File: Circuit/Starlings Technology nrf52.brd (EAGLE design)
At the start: 45.1 x 52.7 mm, 58 parts, among them J4 USB Micro, J7 CORTEX_DEBUG_SMD, Q2 BSS84, U2 MCP73831, U3 BC840M, U4 MIC5317 (MIC5205), U5 74AHCT2G125, U8 TPS61235P, Y2 FC-12M

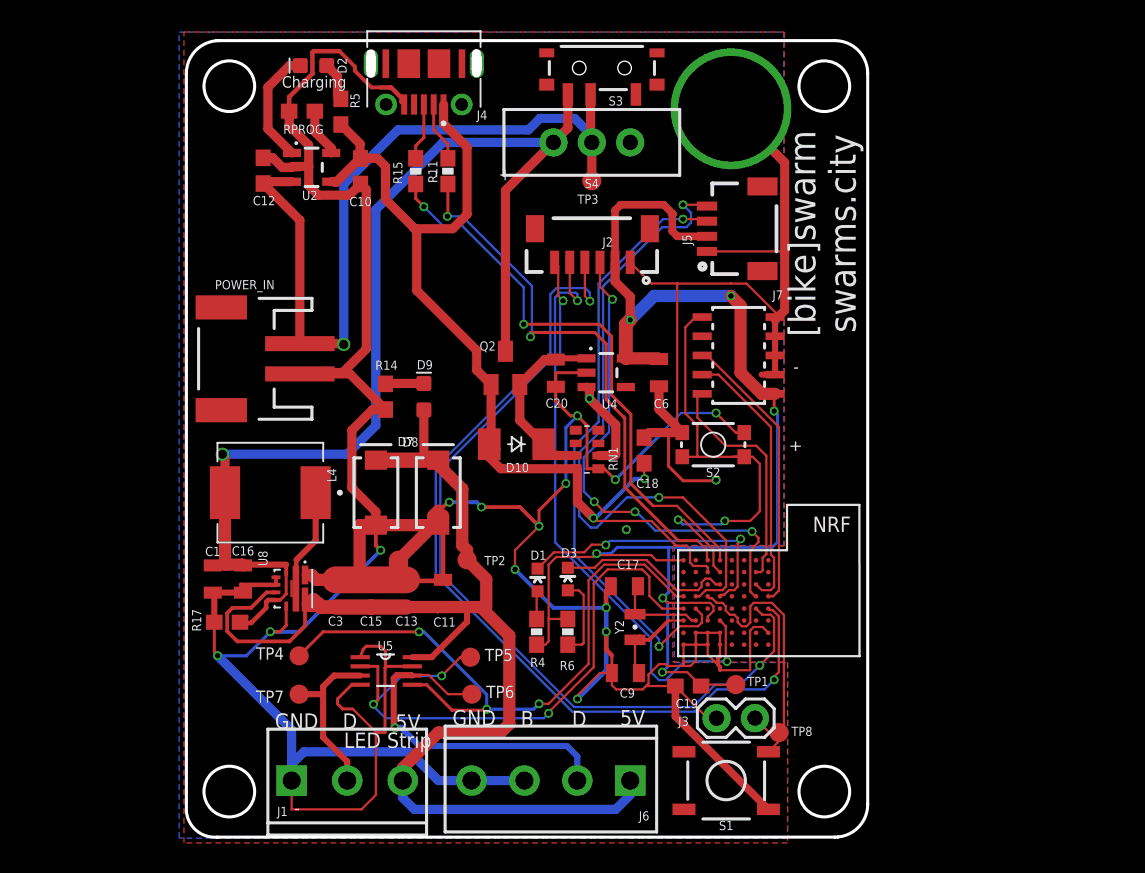
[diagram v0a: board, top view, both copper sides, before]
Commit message: Adding new rocker switch and two tactile switches. Footprints are drawn and ready, just needs routing.
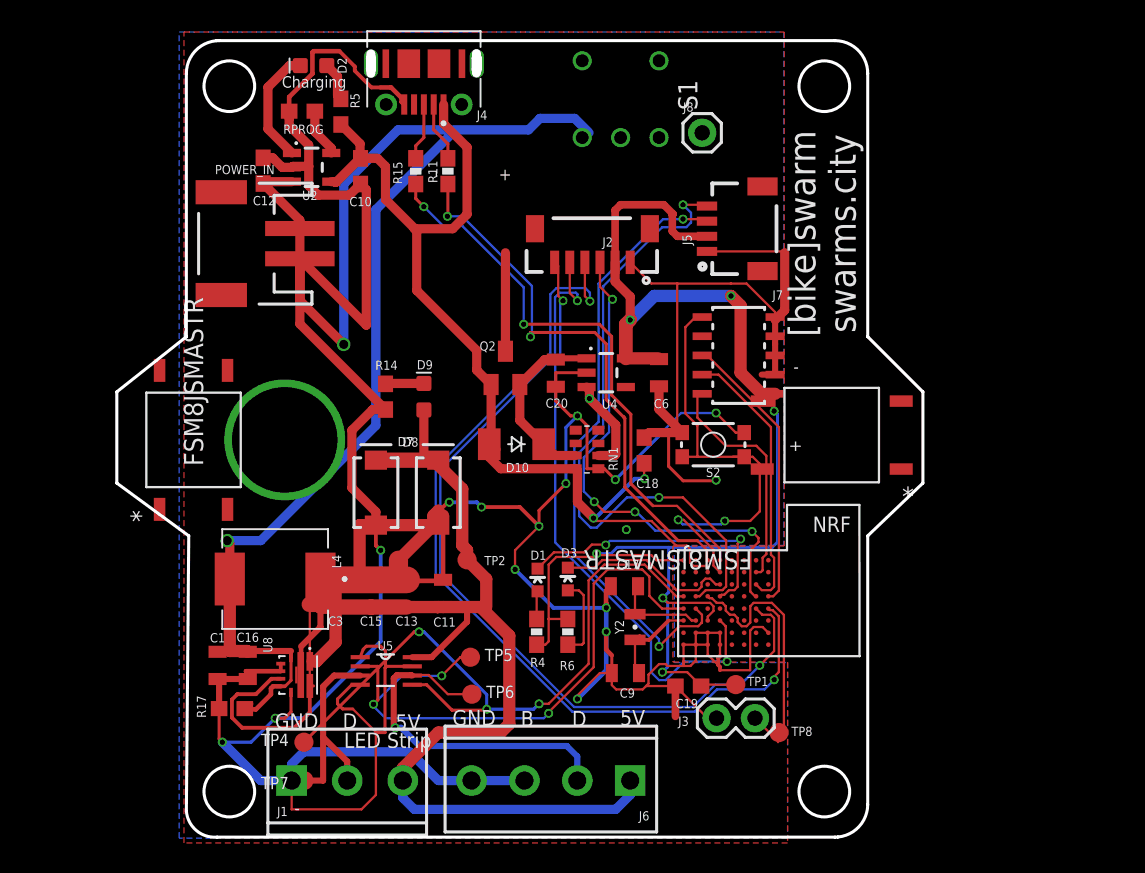
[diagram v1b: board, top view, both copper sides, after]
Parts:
- removed S3: (no value), SparkFun-Switches:SWITCH_SPST_SMD_A
- removed S4: (no value), SparkFun-Switches:SWITCH_SPDT_PTH_11.6X4.0MM
- removed TP3: TPSB1,27, testpad:B1,27
- added J8: (no value), SparkFun-Connectors:1X01
- added SW1, SW2: FSM8JSMASTR, FSM8JSMASTR:SW4_FSM8JSMASTR_TEC
- S1: value SPST-SMD-5.2MM -> CF-LD-1DC4-AR2W; device SparkFun-Switches:TACTILE_SWITCH_SMD_5.2MM -> RA1122DWR:CF-LD-1DC4-AR2W
- moved S1 45.6 mm to (24.8, 49.2), turned to 270 degrees
- moved POWER_IN 7.62 mm to (-0.16, 39.7)
- moved L4 5.72 mm to (1.91, 17.5)
- moved R17 5.72 mm to (-0.95, 8.89)
- moved TP4 5.72 mm to (3.81, 6.67)
- moved U8 5.72 mm to (3.43, 11.1)
- moved TP7 5.72 mm to (3.81, 4.13)
- moved C1 5.72 mm to (-1.91, 11.7)
- moved C16 5.72 mm to (0.10, 11.7)
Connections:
- new net 6: S1.5
- new net SWITCH_2: SW2.3, SW2.4
- net GND: now also SW1.1, SW1.2, SW2.1, SW2.2; no longer S1.1
- net SWITCH_1: now also SW1.3, SW1.4; no longer S1.3
- net VBAT: now also J8.1, S1.3; no longer S3.1, S4.1
- net VBAT_RAW: now also S1.4; no longer S3.2, S4.2, TP3.TP
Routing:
- net VBAT: track 77.8 -> 61.3 mm
- net GND: track 350.6 -> 340.7 mm
- net VBAT_RAW: track 52.1 -> 43.9 mm
- net 5V: track 90.3 -> 95.6 mm
- net HEADLAMP_5V: track 11.2 -> 13.8 mm
- net HEADLAMP_3V3: track 43.6 -> 45.6 mm
- net SWITCH_1: track 19.5 -> 18.6 mm
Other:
- board size 45.1 x 52.7 mm -> 53.3 x 52.7 mm

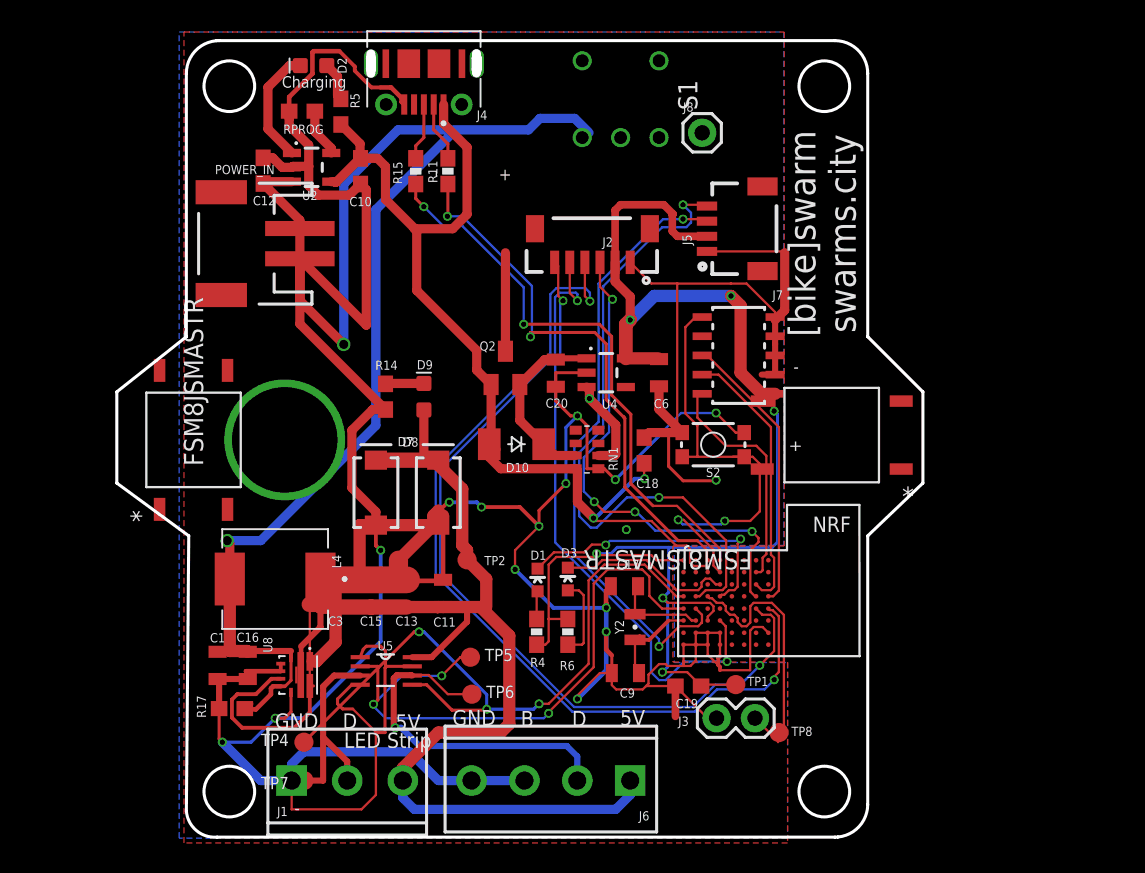
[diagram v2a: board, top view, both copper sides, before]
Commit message: Adjusting dimensions, adding pins to expansion header, connecting second switch.
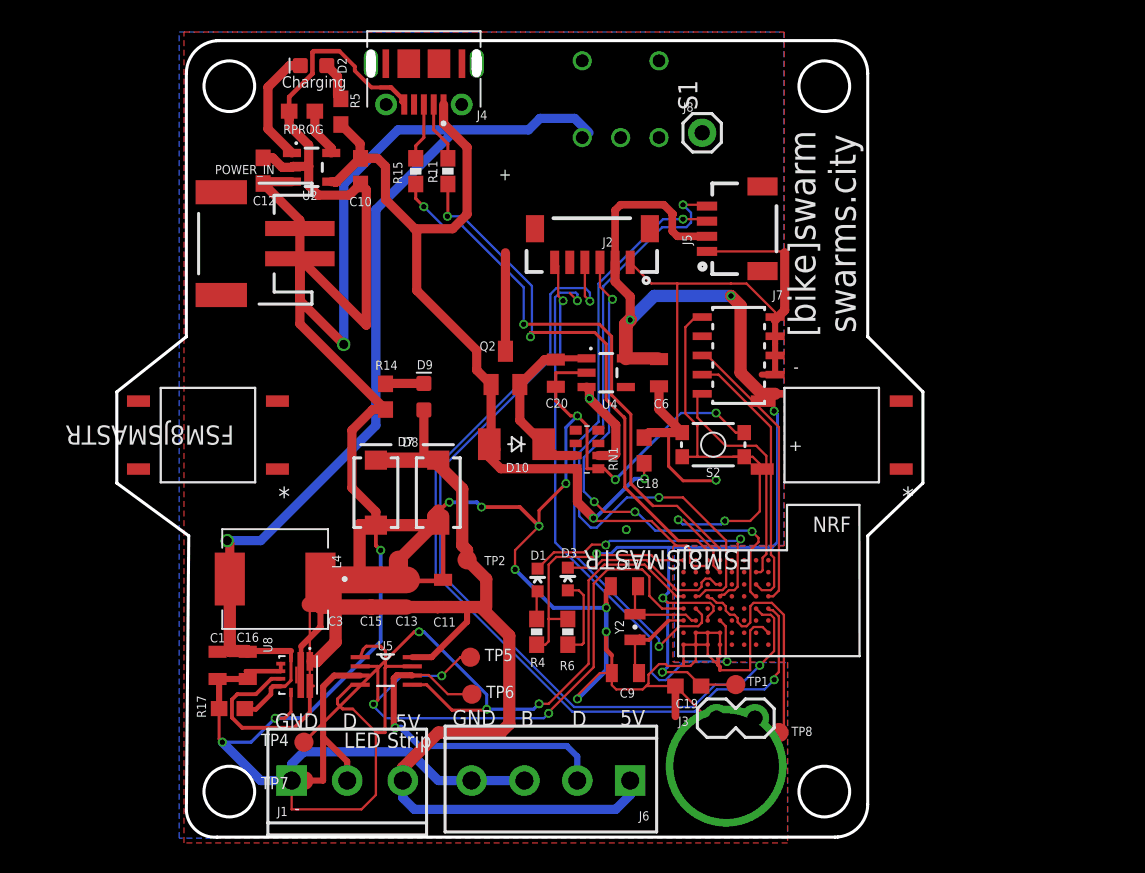
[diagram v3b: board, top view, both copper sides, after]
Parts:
- moved SW1 1.00 mm to (-2.54, 27.0), turned to 180 degrees
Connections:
- net PIN_01: now also U3.G1
- net PIN_02: now also U3.C6
- net PIN_03: now also U3.C7
- net SWITCH_2: now also U3.B7
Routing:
- net PIN_03: track 57.1 -> 55.1 mm
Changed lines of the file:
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@@
 </layers>
 <board>
-<fusionsync huburn="a.YnVzaW5lc3M6b2Zicm9va2x5bg" projecturn="a.YnVzaW5lc3M6b2Zicm9va2x5biMyMDIwMTAwMTMzODU2MDI1Ng" f3durn="urn:adsk.wipprod:dm.lineage:hXMIRU8zTouxHumEHYtLwg" pcbguid="" lastpulledtime="2020-10-19T19:53:36Z" lastsyncedchangeguid="" latestrevisionid="15b58f2b-fb4b-468f-845a-644111b4afad" lastsyncedrevisionid="15b58f2b-fb4b-468f-845a-644111b4afad" lastboardhashguid="4d7612c6-9046-ea51-b418-22ff4dbd317c" lastpushedtime="2022-03-02T20:37:53Z" linktopcb3d="true"/>
+<fusionsync huburn="a.YnVzaW5lc3M6b2Zicm9va2x5bg" projecturn="a.YnVzaW5lc3M6b2Zicm9va2x5biMyMDIwMTAwMTMzODU2MDI1Ng" f3durn="urn:adsk.wipprod:dm.lineage:hXMIRU8zTouxHumEHYtLwg" pcbguid="" lastpulledtime="2020-10-19T19:53:36Z" lastsyncedchangeguid="" latestrevisionid="2cab605c-ff0e-4758-a60a-1f9ac1ab2252" lastsyncedrevisionid="2cab605c-ff0e-4758-a60a-1f9ac1ab2252" lastboardhashguid="16d225a2-b8a0-5d47-a770-6431c6796998" lastpushedtime="2022-03-02T22:39:47Z" linktopcb3d="true"/>
 <plain>
 <text x="2.3495" y="49.9745" size="0.762" layer="21">Charging</text>
@@
 <attribute name="VALUE" x="29.845" y="6.223" size="0.6096" layer="27" font="vector" ratio="20"/>
 </element>
-<element name="SW1" library="FSM8JSMASTR" package="SW4_FSM8JSMASTR_TEC" value="FSM8JSMASTR" x="-3.4925" y="26.67" smashed="yes" rot="R90">
-<attribute name="COPYRIGHT" value="Copyright (C) 2022 Ultra Librarian. All rights reserved." x="-3.4925" y="26.67" size="1.778" layer="27" rot="R90" display="off"/>
-<attribute name="DIGI-KEY_PART_NUMBER_1" value="450-2135-2-ND" x="-3.4925" y="26.67" size="1.778" layer="27" rot="R90" display="off"/>
-<attribute name="DIGI-KEY_PART_NUMBER_2" value="450-2135-1-ND" x="-3.4925" y="26.67" size="1.778" layer="27" rot="R90" display="off"/>
-<attribute name="DIGI-KEY_PART_NUMBER_3" value="450-2135-6-ND" x="-3.4925" y="26.67" size="1.778" layer="27" rot="R90" display="off"/>
-<attribute name="MANUFACTURER_PART_NUMBER" value="FSM8JSMASTR" x="-3.4925" y="26.67" size="1.778" layer="27" rot="R90" display="off"/>
-<attribute name="MFR_NAME" value="TE Connectivity" x="-3.4925" y="26.67" size="1.778" layer="27" rot="R90" display="off"/>
-<attribute name="NAME" x="-2.8575" y="23.3934" size="1.27" layer="27" ratio="6" rot="SR90"/>
-<attribute name="VALUE" x="-2.8575" y="24.9428" size="1.27" layer="21" ratio="6" rot="SR90"/>
+<element name="SW1" library="FSM8JSMASTR" package="SW4_FSM8JSMASTR_TEC" value="FSM8JSMASTR" x="-2.54" y="26.9875" smashed="yes" rot="R180">
+<attribute name="COPYRIGHT" value="Copyright (C) 2022 Ultra Librarian. All rights reserved." x="-2.54" y="26.9875" size="1.778" layer="27" rot="R180" display="off"/>
+<attribute name="DIGI-KEY_PART_NUMBER_1" value="450-2135-2-ND" x="-2.54" y="26.9875" size="1.778" layer="27" rot="R180" display="off"/>
+<attribute name="DIGI-KEY_PART_NUMBER_2" value="450-2135-1-ND" x="-2.54" y="26.9875" size="1.778" layer="27" rot="R180" display="off"/>
+<attribute name="DIGI-KEY_PART_NUMBER_3" value="450-2135-6-ND" x="-2.54" y="26.9875" size="1.778" layer="27" rot="R180" display="off"/>
+<attribute name="MANUFACTURER_PART_NUMBER" value="FSM8JSMASTR" x="-2.54" y="26.9875" size="1.778" layer="27" rot="R180" display="off"/>
+<attribute name="MFR_NAME" value="TE Connectivity" x="-2.54" y="26.9875" size="1.778" layer="27" rot="R180" display="off"/>
+<attribute name="NAME" x="0.7366" y="27.6225" size="1.27" layer="27" ratio="6" rot="SR180"/>
+<attribute name="VALUE" x="-0.8128" y="27.6225" size="1.27" layer="21" ratio="6" rot="SR180"/>
 </element>
 <element name="SW2" library="FSM8JSMASTR" package="SW4_FSM8JSMASTR_TEC" value="FSM8JSMASTR" x="38.735" y="26.9875" smashed="yes" rot="R180">
@@
 <wire x1="3.54125" y1="38.65575" x2="7.9375" y2="34.2595" width="0.6096" layer="1"/>
 <via x="19.3675" y="20.955" extent="1-16" drill="0.35"/>
-<via x="2.54" y="26.67" extent="1-16" drill="6.985"/>
+<via x="31.75" y="5.08" extent="1-16" drill="6.985"/>
 <contactref element="J6" pad="3"/>
 <contactref element="J6" pad="4"/>
@@
 <wire x1="31.115" y1="8.255" x2="30.519" y2="8.255" width="0" layer="19" extent="1-1"/>
 <wire x1="25.146" y1="20.73275" x2="24.41575" y2="24.03475" width="0" layer="19" extent="1-1"/>
-<wire x1="2.54" y1="26.67" x2="5.9055" y2="17.41" width="0" layer="19" extent="1-1"/>
-<wire x1="-1.2446" y1="22.0726" x2="2.54" y2="26.67" width="0" layer="19" extent="1-1"/>
-<wire x1="-5.7404" y1="22.0726" x2="-1.2446" y2="22.0726" width="0" layer="19" extent="1-1"/>
+<wire x1="31.75" y1="5.08" x2="5.9055" y2="17.41" width="0" layer="19" extent="1-1"/>
+<wire x1="2.0574" y1="29.2354" x2="31.75" y2="5.08" width="0" layer="19" extent="1-1"/>
+<wire x1="2.0574" y1="24.7396" x2="2.0574" y2="29.2354" width="0" layer="19" extent="1-1"/>
 </signal>
 <signal name="RESET">
@@
 <contactref element="SW1" pad="3"/>
 <contactref element="SW1" pad="4"/>
-<wire x1="-1.2446" y1="31.2674" x2="30.5276" y2="16.3195" width="0" layer="19" extent="1-1"/>
-<wire x1="-5.7404" y1="31.2674" x2="-1.2446" y2="31.2674" width="0" layer="19" extent="1-1"/>
+<wire x1="-7.1374" y1="29.2354" x2="30.5276" y2="16.3195" width="0" layer="19" extent="1-1"/>
+<wire x1="-7.1374" y1="24.7396" x2="-7.1374" y2="29.2354" width="0" layer="19" extent="1-1"/>
 </signal>
 <signal name="LED_2">
@@
 <wire x1="23.39975" y1="38.41725" x2="23.39975" y2="36.79825" width="0.1524" layer="1"/>
 <wire x1="23.39975" y1="36.79825" x2="24.22525" y2="35.97275" width="0.1524" layer="1"/>
+<contactref element="U3" pad="G1"/>
+<wire x1="33.728" y1="16.3195" x2="33.728" y2="13.9065" width="0" layer="19" extent="1-1"/>
 </signal>
 <signal name="PIN_02">
@@
 <wire x1="22.733" y1="35.84575" x2="22.733" y2="36.4123875" width="0.1524" layer="16"/>
 <wire x1="22.733" y1="36.4123875" x2="22.4324875" y2="36.7129" width="0.1524" layer="16"/>
+<contactref element="U3" pad="C6"/>
+<wire x1="34.5408" y1="15.5067" x2="29.7402" y2="17.1069" width="0" layer="19" extent="1-1"/>
 </signal>
 <signal name="PIN_03">
@@
 <wire x1="21.6877125" y1="8.9944" x2="12.8389" y2="17.8432125" width="0.1524" layer="16"/>
 <wire x1="12.8389" y1="24.69995625" x2="12.8389" y2="17.8432125" width="0.1524" layer="16"/>
-<wire x1="21.4" y1="38.4175" x2="21.4" y2="36.385" width="0.1524" layer="1"/>
 <wire x1="21.9075" y1="35.8775" x2="21.4" y2="36.385" width="0.1524" layer="1"/>
 <wire x1="20.4244" y1="36.0972875" x2="20.7352125" y2="36.4081" width="0.1524" layer="16"/>
@@
 <wire x1="21.8097875" y1="36.4081" x2="21.9075" y2="36.3103875" width="0.1524" layer="16"/>
 <wire x1="21.9075" y1="36.3103875" x2="21.9075" y2="35.8775" width="0.1524" layer="16"/>
+<contactref element="U3" pad="C7"/>
+<wire x1="21.4" y1="36.385" x2="21.4" y2="38.4175" width="0" layer="19" extent="1-1"/>
+<wire x1="28.9274" y1="17.1069" x2="33.728" y2="15.5067" width="0" layer="19" extent="1-1"/>
 </signal>
 <signal name="PIN_04">
@@
 <contactref element="SW2" pad="4"/>
 <contactref element="SW2" pad="3"/>
+<contactref element="U3" pad="B7"/>
 <wire x1="34.1376" y1="24.7396" x2="34.1376" y2="29.2354" width="0" layer="19" extent="1-1"/>
+<wire x1="28.9274" y1="17.9197" x2="34.1376" y2="24.7396" width="0" layer="19" extent="1-1"/>
 </signal>
 <signal name="6">
@@
 <mfgpreviewcolor name="substratecolor" color="0xFF786E46"/>
 </mfgpreviewcolors>
-<errors>
-</errors>
 </board>
 </drawing>
